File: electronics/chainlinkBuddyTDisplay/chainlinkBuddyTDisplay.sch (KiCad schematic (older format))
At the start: 7 parts, among them J1 Output, J2 Screw_Terminal_01x03, U1 TTGO_TDisplay

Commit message: Chainlink Buddy T-Display prep
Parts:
- added C1: 10uF, Capacitor_SMD:C_1206_3216Metric_Pad1.33x1.80mm_HandSolder, symbol Device:C_Small
- added C2: 22uF, Capacitor_SMD:C_1206_3216Metric_Pad1.33x1.80mm_HandSolder, symbol Device:C_Small
- added J3: Barrel_Jack_Switch, PJ-202A:PJ-202A, symbol Connector:Barrel_Jack_Switch
- added U2: LM7805_TO220, ModifiedSymbols:TO-220-3_Vertical, symbol Regulator_Linear:LM7805_TO220
- added Z1: polarity label, Symbol:Symbol_Barrel_Polarity, symbol no_pin:no_pin
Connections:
- net +5V: now also C2.1, U2.3 (VO); no longer J2.3 (Pin_3)
- net GND: now also C1.2, C2.2, J3.2, U2.2 (GND)
- new net +12V: C1.1, J2.3 (Pin_3), J3.1, U2.1 (VI)
- no-connect marks 13 -> 14
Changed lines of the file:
@@
 	2500 3100 2500 3900
 $Comp
-L power:+5V #PWR0105
-U 1 1 61A81BDD
+L power:+5V #PWR0106
+U 1 1 61A82D03
 P 3950 4000
-F 0 "#PWR0105" H 3950 3850 50  0001 C CNN
+F 0 "#PWR0106" H 3950 3850 50  0001 C CNN
 F 1 "+5V" H 3965 4173 50  0000 C CNN
 F 2 "" H 3950 4000 50  0001 C CNN
 F 3 "" H 3950 4000 50  0001 C CNN
 	1    3950 4000
-	1    0    0    -1
-$EndComp
-Wire Wire Line
-	3650 4100 3950 4100
-Wire Wire Line
-	3950 4100 3950 4000
-$Comp
-L power:+5V #PWR0106
-U 1 1 61A82D03
-P 4500 4550
-F 0 "#PWR0106" H 4500 4400 50  0001 C CNN
-F 1 "+5V" H 4515 4723 50  0000 C CNN
-F 2 "" H 4500 4550 50  0001 C CNN
-F 3 "" H 4500 4550 50  0001 C CNN
-	1    4500 4550
 	1    0    0    -1
 $EndComp
@@
 NoConn ~ 3650 3100
 NoConn ~ 3650 3000
+$Comp
+L Connector:Barrel_Jack_Switch J3
+U 1 1 617CEDE5
+P 1500 1750
+F 0 "J3" H 1557 2067 50  0000 C CNN
+F 1 "Barrel_Jack_Switch" H 1557 1976 50  0000 C CNN
+F 2 "PJ-202A:PJ-202A" H 1550 1710 50  0001 C CNN
+F 3 "~" H 1550 1710 50  0001 C CNN
+	1    1500 1750
+	1    0    0    -1
+$EndComp
+$Comp
+L power:+12V #PWR02
+U 1 1 617D49A3
+P 1950 1550
+F 0 "#PWR02" H 1950 1400 50  0001 C CNN
+F 1 "+12V" H 1965 1723 50  0000 C CNN
+F 2 "" H 1950 1550 50  0001 C CNN
+F 3 "" H 1950 1550 50  0001 C CNN
+	1    1950 1550
+	1    0    0    -1
+$EndComp
+Wire Wire Line
+	1800 1650 1950 1650
+Wire Wire Line
+	1950 1650 1950 1550
+$Comp
+L power:GND #PWR05
+U 1 1 617D5F7C
+P 1950 2000
+F 0 "#PWR05" H 1950 1750 50  0001 C CNN
+F 1 "GND" H 1955 1827 50  0000 C CNN
+F 2 "" H 1950 2000 50  0001 C CNN
+F 3 "" H 1950 2000 50  0001 C CNN
+	1    1950 2000
+	1    0    0    -1
+$EndComp
+Wire Wire Line
+	1800 1850 1950 1850
+Wire Wire Line
+	1950 1850 1950 2000
+NoConn ~ 1800 1750
+$Comp
+L Regulator_Linear:LM7805_TO220 U2
+U 1 1 617DC13F
+P 3750 1650
+F 0 "U2" H 3750 1892 50  0000 C CNN
+F 1 "LM7805_TO220" H 3750 1801 50  0000 C CNN
+F 2 "ModifiedSymbols:TO-220-3_Vertical" H 3750 1875 50  0001 C CIN
+F 3 "https://www.onsemi.cn/PowerSolutions/document/MC7800-D.PDF" H 3750 1600 50  0001 C CNN
+	1    3750 1650
+	1    0    0    -1
+$EndComp
+$Comp
+L Device:C_Small C1
+U 1 1 617DDA1A
+P 3300 1750
+F 0 "C1" H 3250 2000 50  0000 L CNN
+F 1 "10uF" H 3150 1950 50  0000 L CNN
+F 2 "Capacitor_SMD:C_1206_3216Metric_Pad1.33x1.80mm_HandSolder" H 3300 1750 50  0001 C CNN
+F 3 "~" H 3300 1750 50  0001 C CNN
+	1    3300 1750
+	1    0    0    -1
+$EndComp
+Wire Wire Line
+	3300 1650 3450 1650
+Wire Wire Line
+	3300 1850 3300 1950
+Wire Wire Line
+	3300 1950 3750 1950
+$Comp
+L Device:C_Small C2
+U 1 1 617E09DF
+P 4250 1750
+F 0 "C2" H 4200 2000 50  0000 L CNN
+F 1 "22uF" H 4100 1950 50  0000 L CNN
+F 2 "Capacitor_SMD:C_1206_3216Metric_Pad1.33x1.80mm_HandSolder" H 4250 1750 50  0001 C CNN
+F 3 "~" H 4250 1750 50  0001 C CNN
+	1    4250 1750
+	1    0    0    -1
+$EndComp
+Wire Wire Line
+	4250 1850 4250 1950
+Wire Wire Line
+	4250 1950 3750 1950
+Connection ~ 3750 1950
+Wire Wire Line
+	4050 1650 4250 1650
+$Comp
+L power:+12V #PWR03
+U 1 1 617E2C4F
+P 3000 1650
+F 0 "#PWR03" H 3000 1500 50  0001 C CNN
+F 1 "+12V" H 3015 1823 50  0000 C CNN
+F 2 "" H 3000 1650 50  0001 C CNN
+F 3 "" H 3000 1650 50  0001 C CNN
+	1    3000 1650
+	1    0    0    -1
+$EndComp
+Wire Wire Line
+	3000 1650 3300 1650
+Connection ~ 3300 1650
+$Comp
+L power:+5V #PWR04
+U 1 1 617E4049
+P 4550 1650
+F 0 "#PWR04" H 4550 1500 50  0001 C CNN
+F 1 "+5V" H 4565 1823 50  0000 C CNN
+F 2 "" H 4550 1650 50  0001 C CNN
+F 3 "" H 4550 1650 50  0001 C CNN
+	1    4550 1650
+	1    0    0    -1
+$EndComp
+Wire Wire Line
+	4550 1650 4250 1650
+Connection ~ 4250 1650
+$Comp
+L power:GND #PWR06
+U 1 1 617E548E
+P 3750 2050
+F 0 "#PWR06" H 3750 1800 50  0001 C CNN
+F 1 "GND" H 3755 1877 50  0000 C CNN
+F 2 "" H 3750 2050 50  0001 C CNN
+F 3 "" H 3750 2050 50  0001 C CNN
+	1    3750 2050
+	1    0    0    -1
+$EndComp
+Wire Wire Line
+	3750 2050 3750 1950
+Wire Wire Line
+	3950 4000 3950 4100
+Wire Wire Line
+	3950 4100 3650 4100
+$Comp
+L power:+12V #PWR07
+U 1 1 617EBE63
+P 4500 4550
+F 0 "#PWR07" H 4500 4400 50  0001 C CNN
+F 1 "+12V" H 4515 4723 50  0000 C CNN
+F 2 "" H 4500 4550 50  0001 C CNN
+F 3 "" H 4500 4550 50  0001 C CNN
+	1    4500 4550
+	1    0    0    -1
+$EndComp
+$Comp
+L no_pin:no_pin Z1
+U 1 1 617F16BD
+P 1550 1150
+F 0 "Z1" H 1550 1437 60  0000 C CNN
+F 1 "polarity label" H 1550 1331 60  0000 C CNN
+F 2 "Symbol:Symbol_Barrel_Polarity" H 1550 1150 60  0001 C CNN
+F 3 "" H 1550 1150 60  0001 C CNN
+	1    1550 1150
+	1    0    0    -1
+$EndComp
+$Comp
+L power:PWR_FLAG #FLG0101
+U 1 1 617F3266
+P 2250 1650
+F 0 "#FLG0101" H 2250 1725 50  0001 C CNN
+F 1 "PWR_FLAG" H 2250 1823 50  0000 C CNN
+F 2 "" H 2250 1650 50  0001 C CNN
+F 3 "~" H 2250 1650 50  0001 C CNN
+	1    2250 1650
+	1    0    0    -1
+$EndComp
+$Comp
+L power:PWR_FLAG #FLG0102
+U 1 1 617F36A9
+P 2250 1850
+F 0 "#FLG0102" H 2250 1925 50  0001 C CNN
+F 1 "PWR_FLAG" H 2250 2023 50  0000 C CNN
+F 2 "" H 2250 1850 50  0001 C CNN
+F 3 "~" H 2250 1850 50  0001 C CNN
+	1    2250 1850
+	1    0    0    -1
+$EndComp
+Wire Wire Line
+	1950 1850 2250 1850
+Connection ~ 1950 1850
+Wire Wire Line
+	1950 1650 2250 1650
+Connection ~ 1950 1650
+$Comp
+L power:PWR_FLAG #FLG0103
+U 1 1 617F6261
+P 2000 4100
+F 0 "#FLG0103" H 2000 4175 50  0001 C CNN
+F 1 "PWR_FLAG" H 2000 4273 50  0000 C CNN
+F 2 "" H 2000 4100 50  0001 C CNN
+F 3 "~" H 2000 4100 50  0001 C CNN
+	1    2000 4100
+	1    0    0    -1
+$EndComp
+Wire Wire Line
+	2000 4100 2250 4100
+Connection ~ 2250 4100
 $EndSCHEMATC

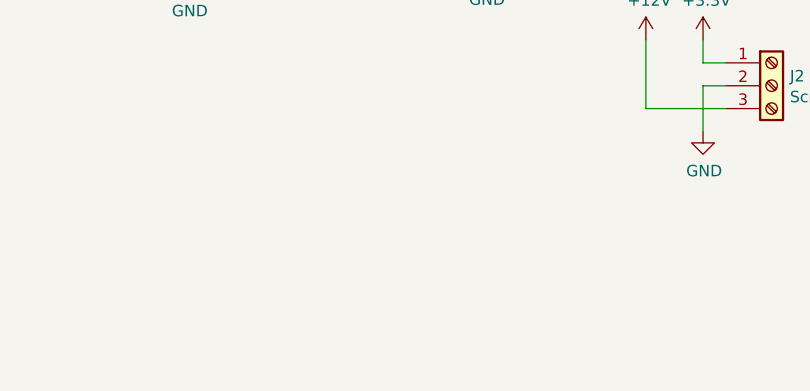
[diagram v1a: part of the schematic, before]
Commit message: Add spare 12V pins to Chainlink Buddy T-Display
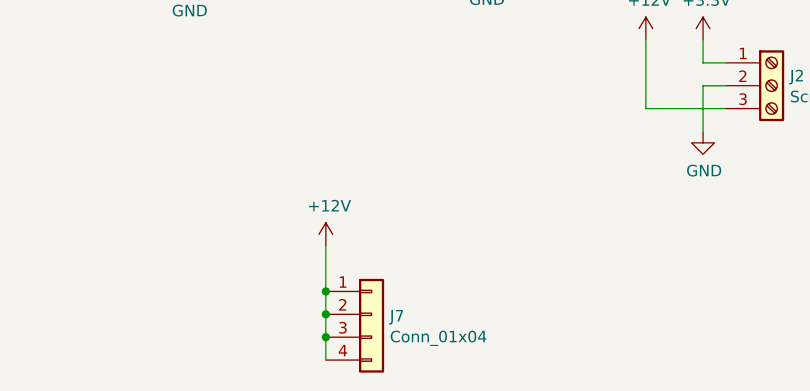
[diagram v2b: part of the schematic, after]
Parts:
- added J7: Conn_01x04, ModifiedSymbols:PinHoles_1x04_P2.54mm_NoSilk, symbol Connector_Generic:Conn_01x04
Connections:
- net +12V: now also J7.1 (Pin_1), J7.2 (Pin_2), J7.3 (Pin_3), J7.4 (Pin_4)
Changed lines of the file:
@@
 	2000 4100 2250 4100
 Connection ~ 2250 4100
+$Comp
+L Connector_Generic:Conn_01x04 J7
+U 1 1 61C9DDB1
+P 3300 5750
+F 0 "J7" H 3380 5742 50  0000 L CNN
+F 1 "Conn_01x04" H 3380 5651 50  0000 L CNN
+F 2 "ModifiedSymbols:PinHoles_1x04_P2.54mm_NoSilk" H 3300 5750 50  0001 C CNN
+F 3 "~" H 3300 5750 50  0001 C CNN
+	1    3300 5750
+	1    0    0    -1
+$EndComp
+Wire Wire Line
+	3100 5450 3100 5650
+Connection ~ 3100 5650
+Wire Wire Line
+	3100 5650 3100 5750
+Connection ~ 3100 5750
+Wire Wire Line
+	3100 5750 3100 5850
+Connection ~ 3100 5850
+Wire Wire Line
+	3100 5850 3100 5950
+$Comp
+L power:+12V #PWR0111
+U 1 1 61CA0D35
+P 3100 5450
+F 0 "#PWR0111" H 3100 5300 50  0001 C CNN
+F 1 "+12V" H 3115 5623 50  0000 C CNN
+F 2 "" H 3100 5450 50  0001 C CNN
+F 3 "" H 3100 5450 50  0001 C CNN
+	1    3100 5450
+	1    0    0    -1
+$EndComp
 $EndSCHEMATC

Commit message: More tweaks to Chainlink Driver, update Chainlink Buddy
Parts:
- J1: footprint ModifiedSymbols:IDC-Header_2x04_P2.54mm_Vertical -> ModifiedSymbols:IDC-Header_2x05_P2.54mm_Vertical_2x04Silk; symbol Connector_Generic:Conn_02x04_Odd_Even -> Connector_Generic:Conn_02x05_Odd_Even
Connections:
- net GND: now also J1.10 (Pin_10)
- net nOE: now reaches U1.16 (GPIO26)
- net nOE: now also J1.9 (Pin_9)
- no-connect marks 14 -> 13
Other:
- note added: "Older versions of the Chainlink system\nused a 2x4 IDC connector and 8-pin\nribbon cable, omitting the output-enable \nsignal + GND on pins 9 and 10.\n\nFor backwards compatibility, you may use\na 2x4 IDC connector connected only to\npins 1-8."
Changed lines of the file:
@@
 $EndComp
 $Comp
-L Connector_Generic:Conn_02x04_Odd_Even J1
+L Connector_Generic:Conn_02x05_Odd_Even J1
 U 1 1 61A3A5EC
-P 6700 3400
-F 0 "J1" H 6750 3717 50  0000 C CNN
-F 1 "Output" H 6750 3626 50  0000 C CNN
-F 2 "ModifiedSymbols:IDC-Header_2x04_P2.54mm_Vertical" H 6700 3400 50  0001 C CNN
-F 3 "~" H 6700 3400 50  0001 C CNN
-	1    6700 3400
+P 6700 3500
+F 0 "J1" H 6750 3817 50  0000 C CNN
+F 1 "Output" H 6750 3900 50  0000 C CNN
+F 2 "ModifiedSymbols:IDC-Header_2x05_P2.54mm_Vertical_2x04Silk" H 6700 3500 50  0001 C CNN
+F 3 "~" H 6700 3500 50  0001 C CNN
+	1    6700 3500
 	1    0    0    -1
 $EndComp
@@
 $EndComp
 Wire Wire Line
-	7000 3600 7000 3750
+	7000 3600 7000 3700
 Wire Wire Line
 	7000 3300 7000 3400
@@
 L power:+5V #PWR0106
 U 1 1 61A82D03
-P 3950 4000
-F 0 "#PWR0106" H 3950 3850 50  0001 C CNN
-F 1 "+5V" H 3965 4173 50  0000 C CNN
-F 2 "" H 3950 4000 50  0001 C CNN
-F 3 "" H 3950 4000 50  0001 C CNN
-	1    3950 4000
+P 3950 4050
+F 0 "#PWR0106" H 3950 3900 50  0001 C CNN
+F 1 "+5V" H 3965 4223 50  0000 C CNN
+F 2 "" H 3950 4050 50  0001 C CNN
+F 3 "" H 3950 4050 50  0001 C CNN
+	1    3950 4050
 	1    0    0    -1
 $EndComp
@@
 NoConn ~ 2650 3800
 NoConn ~ 3650 3900
-NoConn ~ 3650 3800
 NoConn ~ 3650 3300
 NoConn ~ 3650 3200
@@
 	3750 2050 3750 1950
 Wire Wire Line
-	3950 4000 3950 4100
-Wire Wire Line
 	3950 4100 3650 4100
 $Comp
@@
 	1    0    0    -1
 $EndComp
+Wire Wire Line
+	7000 3750 7000 3700
+Connection ~ 7000 3700
+Text Label 5900 3700 0    50   ~ 0
+nOE
+Wire Wire Line
+	6500 3700 5900 3700
+Wire Wire Line
+	3650 3800 4400 3800
+Text Label 4400 3800 2    50   ~ 0
+nOE
+Wire Wire Line
+	3950 4050 3950 4100
+Text Notes 7150 3800 0    50   ~ 0
+Older versions of the Chainlink system\nused a 2x4 IDC connector and 8-pin\nribbon cable, omitting the output-enable \nsignal + GND on pins 9 and 10.\n\nFor backwards compatibility, you may use\na 2x4 IDC connector connected only to\npins 1-8.
 $EndSCHEMATC
